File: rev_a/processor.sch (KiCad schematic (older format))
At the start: 1 part

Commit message: More work on processor schematic.
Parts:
- added C? (x2): C_VERT, symbol C_VERT
- added J?: TERMINATE_JUMPER, symbol TERMINATE_JUMPER
- added N?: BUS_MASTER_HEADER, symbol BUS_MASTER_HEADER
- added N?: FTDI_HEADER, symbol FTDI_HEADER
- added R? (x3): R_VERT, symbol R_VERT
- added R? (x3): R_HORIZ, symbol R_HORIZ
- added U?: MCP2562, symbol MCP2562
- added U? (x2): 74x06, symbol 74x06
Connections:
- net A1: now also U?.21 (PD7/OC2A)
- net D0: now also R?.2
- net D1: now also R?.2
- net D5: now also U?.18 (PD4/OC1B)
- net GND: now also U?.7 (GND), U?.7 (GND)
- net at U?.16 (PD2/RXD1/INT0): now also U?.1, U?.1 (TXD)
- net at U?.17 (PD3/TXD1/INT1): now also U?.4 (RXD)
- net at U?.9 (~RESET): now also C?.1, N?.6 (~RTS), R?.1, U?.2
- new net: N?.1 (LPWR1), N?.2 (LPWR2)
- new net: N?.10 (BPWR2), N?.9 (BPWR1)
- new net: N?.3 (LGND1), N?.4 (LGND2)
- new net: J?.1 (ON), N?.5 (CANH), U?.7 (CANH)
- new net: N?.6 (CANL), R?.2, U?.6 (CANL)
- new net: N?.7 (BGND1), N?.8 (BGND2)
- new net: R?.1, U?.2
- new net: C?.1, R?.1, R?.2, U?.1
- new net: N?.4 (TXD), R?.1
- new net: N?.5 (RXD), R?.1
- new net: J?.2 (COM), R?.1
- new net VCC: U?.14 (VCC), U?.14 (VCC)
- no-connect marks 0 -> 3

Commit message: Added some more symbols to library.
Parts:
- added H? (x4): 3MM_HOLE, symbol 3MM_HOLE
- added N? (x2): POWER_TERMINAL, symbol POWER_TERMINAL
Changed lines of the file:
@@
 NoConn ~ 1300 2900
 NoConn ~ 1300 5000
+$Comp
+L 3MM_HOLE H?
+U 1 1 53933893
+P 9800 4700
+F 0 "H?" H 9750 4850 50  0000 C CNN
+F 1 "3MM_HOLE" H 9800 4550 50  0000 C CNN
+F 2 "" H 9800 4700 60  0000 C CNN
+F 3 "" H 9800 4700 60  0000 C CNN
+	1    9800 4700
+	1    0    0    -1
+$EndComp
+$Comp
+L 3MM_HOLE H?
+U 1 1 539338AF
+P 9800 5100
+F 0 "H?" H 9750 5250 50  0000 C CNN
+F 1 "3MM_HOLE" H 9800 4950 50  0000 C CNN
+F 2 "" H 9800 5100 60  0000 C CNN
+F 3 "" H 9800 5100 60  0000 C CNN
+	1    9800 5100
+	1    0    0    -1
+$EndComp
+$Comp
+L 3MM_HOLE H?
+U 1 1 539338BA
+P 9800 5500
+F 0 "H?" H 9750 5650 50  0000 C CNN
+F 1 "3MM_HOLE" H 9800 5350 50  0000 C CNN
+F 2 "" H 9800 5500 60  0000 C CNN
+F 3 "" H 9800 5500 60  0000 C CNN
+	1    9800 5500
+	1    0    0    -1
+$EndComp
+$Comp
+L 3MM_HOLE H?
+U 1 1 539338C5
+P 9800 5900
+F 0 "H?" H 9750 6050 50  0000 C CNN
+F 1 "3MM_HOLE" H 9800 5750 50  0000 C CNN
+F 2 "" H 9800 5900 60  0000 C CNN
+F 3 "" H 9800 5900 60  0000 C CNN
+	1    9800 5900
+	1    0    0    -1
+$EndComp
+$Comp
+L POWER_TERMINAL N?
+U 1 1 539338DC
+P 9800 3750
+F 0 "N?" H 9750 3900 50  0000 C CNN
+F 1 "POWER_TERMINAL" H 9800 3600 50  0000 C CNN
+F 2 "" H 9800 3750 60  0000 C CNN
+F 3 "" H 9800 3750 60  0000 C CNN
+	1    9800 3750
+	1    0    0    -1
+$EndComp
+$Comp
+L POWER_TERMINAL N?
+U 1 1 539338EE
+P 9800 3350
+F 0 "N?" H 9750 3500 50  0000 C CNN
+F 1 "POWER_TERMINAL" H 9800 3200 50  0000 C CNN
+F 2 "" H 9800 3350 60  0000 C CNN
+F 3 "" H 9800 3350 60  0000 C CNN
+	1    9800 3350
+	1    0    0    -1
+$EndComp
 $EndSCHEMATC

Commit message: Making progress on processor sheet.
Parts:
- removed C?: C_VERT, symbol C_VERT
- removed N? (x2): POWER_TERMINAL, symbol POWER_TERMINAL
- added C? (x2): 18pF, symbol C_VERT
- added C?: .1uF, symbol C_HORIZ
- added C? (x3): .1uF, symbol C_VERT
- added D?: SCHOTTKY_DIODE_VERT, symbol SCHOTTKY_DIODE_VERT
- added R?: 1K, symbol R_VERT
- added SW?: 2_LEAD_PUSH_BUTTON, symbol 2_LEAD_PUSH_BUTTON
- added U? (x2): LM2940, symbol LM2940
- added X?: 16MHz, symbol CRYSTAL
- C?: value C_VERT -> .1uF
- R? (x2): value R_VERT -> 10K
- R?: value R_HORIZ -> 180
- R?: value R_VERT -> 120 1%
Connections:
- net labels added: +3.3V, +5V
- wire segments 129 -> 168
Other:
- moved on the sheet: C?, J?, N?, R?, U?, U?A

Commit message: Initial mounting hole layout is done.
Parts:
- removed N?: BUS_MASTER_HEADER, symbol BUS_MASTER_HEADER
- removed N?: FTDI_HEADER, symbol FTDI_HEADER
- removed U?: ATMEGA324_DIP40, symbol ATMEGA324_DIP40
- removed U?: MCP2562, symbol MCP2562
- removed U? (x2): LM2940, symbol LM2940
- added N8: BUS_SLAVE_HEADER, symbol BUS_SLAVE_HEADER
- added N9: FTDI_HEADER, symbol FTDI_HEADER
- added U1, U3: VOLTAGE_REGULATOR, symbol VOLTAGE_REGULATOR
- added U2: MCP2562, symbol MCP2562
- added U5: ATMEGA324_DIP40, symbol ATMEGA324_DIP40
- H6: renamed from H?; value 3MM_HOLE -> BASE_NE_3MM_HOLE
- H7: renamed from H?; value 3MM_HOLE -> BASE_NW_3MM_HOLE
- H8: renamed from H?; value 3MM_HOLE -> BASE_SE_3MM_HOLE
- H9: renamed from H?; value 3MM_HOLE -> BASE_SW_3MM_HOLE
- gave numbers to parts that had none: 19
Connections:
- net VCC is gone; now on net +5V: U4.14 (VCC), U4.14 (VCC)
- net +3.3V: now also U3.3 (VOUT)
- net +5V: now also U1.3 (VOUT), U2.3 (VDD), U2.5 (VIO), U3.1 (VIN), U5.10 (VCC), U5.30 (AVCC)
- net A0: now also U5.40 (PA0/ADC0)
- net A1: now also U5.39 (PA1/ADC1)
- net A2: now also U5.38 (PA2/ADC2)
- net A3: now also U5.37 (PA3/ADC3)
- net A4: now also U5.23 (PC1/SDA), U5.36 (PA4/ADC4)
- net A5: now also U5.22 (PC0/SCL), U5.35 (PA5/ADC5)
- net AREF: now also U5.32 (AREF)
- net D0: now also U5.14 (PD0/RXD0)
- net D1: now also U5.15 (PD1/TXD0)
- net D10: now also U5.5 (PB4/OC0B/SS)
- net D11: now also U5.6 (PB5/MOSI)
- net D12: now also U5.7 (PB6/MISO)
- net D13: now also U5.8 (PB7/SCK)
- net D2: now also U5.3 (PB2/INT2)
- net D3: now also U5.20 (PD6/OC2B)
- net D4: now also U5.1 (PB0/T0)
- net D5: now also U5.18 (PD4/OC1B), U5.2 (PB1/T1)
- net D6: now also U5.4 (PB3/OC0A)
- net D7: now also U5.34 (PA6/ADC6)
- net D8: now also U5.33 (PA7/ADC7)
- net D9: now also U5.19 (PD5/OC1A)
- net GND: now also N8.3 (LGND1), N8.4 (LGND2), N9.1 (GND), U1.2, U2.2 (VSS), U2.8 (STBY), U3.2, U5.11 (GND), U5.31 (GND)
- net MGND: now also N8.10 (BPWR2), N8.9 (BPWR1)
- net MPWR: now also N8.7 (BGND1), N8.8 (BGND2)
- net VIN: now also N8.1 (LPWR1), N8.2 (LPWR2), U1.1 (VIN)
- net ~RESET: now also U4.4, U5.9 (~RESET); no longer U4.2
- net at C2.1, X1.1: now also U5.12 (XTAL2)
- net at C4.1, X1.2: now also U5.13 (XTAL1)
- net at R3.2, U4.1: now also U2.1 (TXD), U5.16 (PD2/RXD1/INT0)
- net at R2.2: now also U2.4 (RXD), U5.17 (PD3/TXD1/INT1)
- net at J1.2 (COM): now also N8.5 (CANH), U2.7 (CANH)
- net at R1.2: now also N8.6 (CANL), U2.6 (CANL)
- net at C7.1, R5.2, R6.1: now also U4.3; no longer U4.1
- net at R3.1: now also N9.4 (TXD)
- net at R2.1: now also N9.5 (RXD)
- net at C6.1, R4.2: now also N9.6 (~RTS)
- no-connect marks 3 -> 10

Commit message: Worked on board.
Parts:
- R2, R3: value R_HORIZ -> 1K
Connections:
- net D0: now also R3.2
- net D1: now also R2.2
- net at U2.1 (TXD), U4.1, U5.16 (PD2/RXD1/INT0): no longer R3.2
- net at U2.4 (RXD), U5.17 (PD3/TXD1/INT1): no longer R2.2
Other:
- moved on the sheet: C1, C2, C3, C4, C5, N9, R2, R3, R4, U1, U3, X1

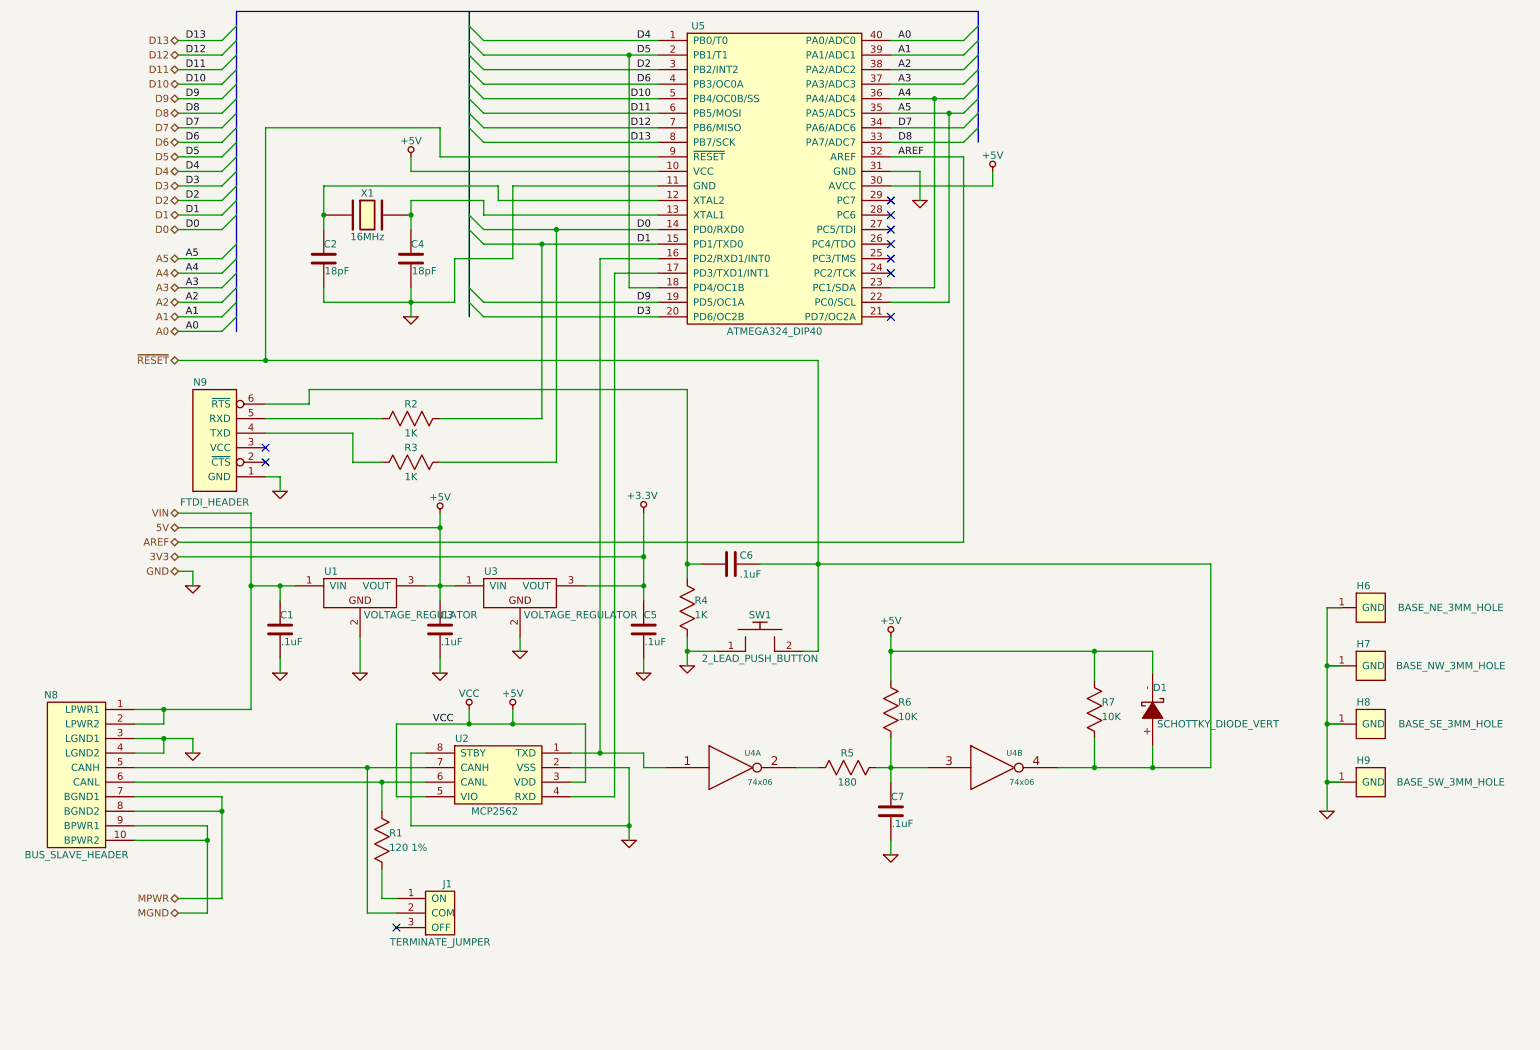
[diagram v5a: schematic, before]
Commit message: Busino passes DRC.
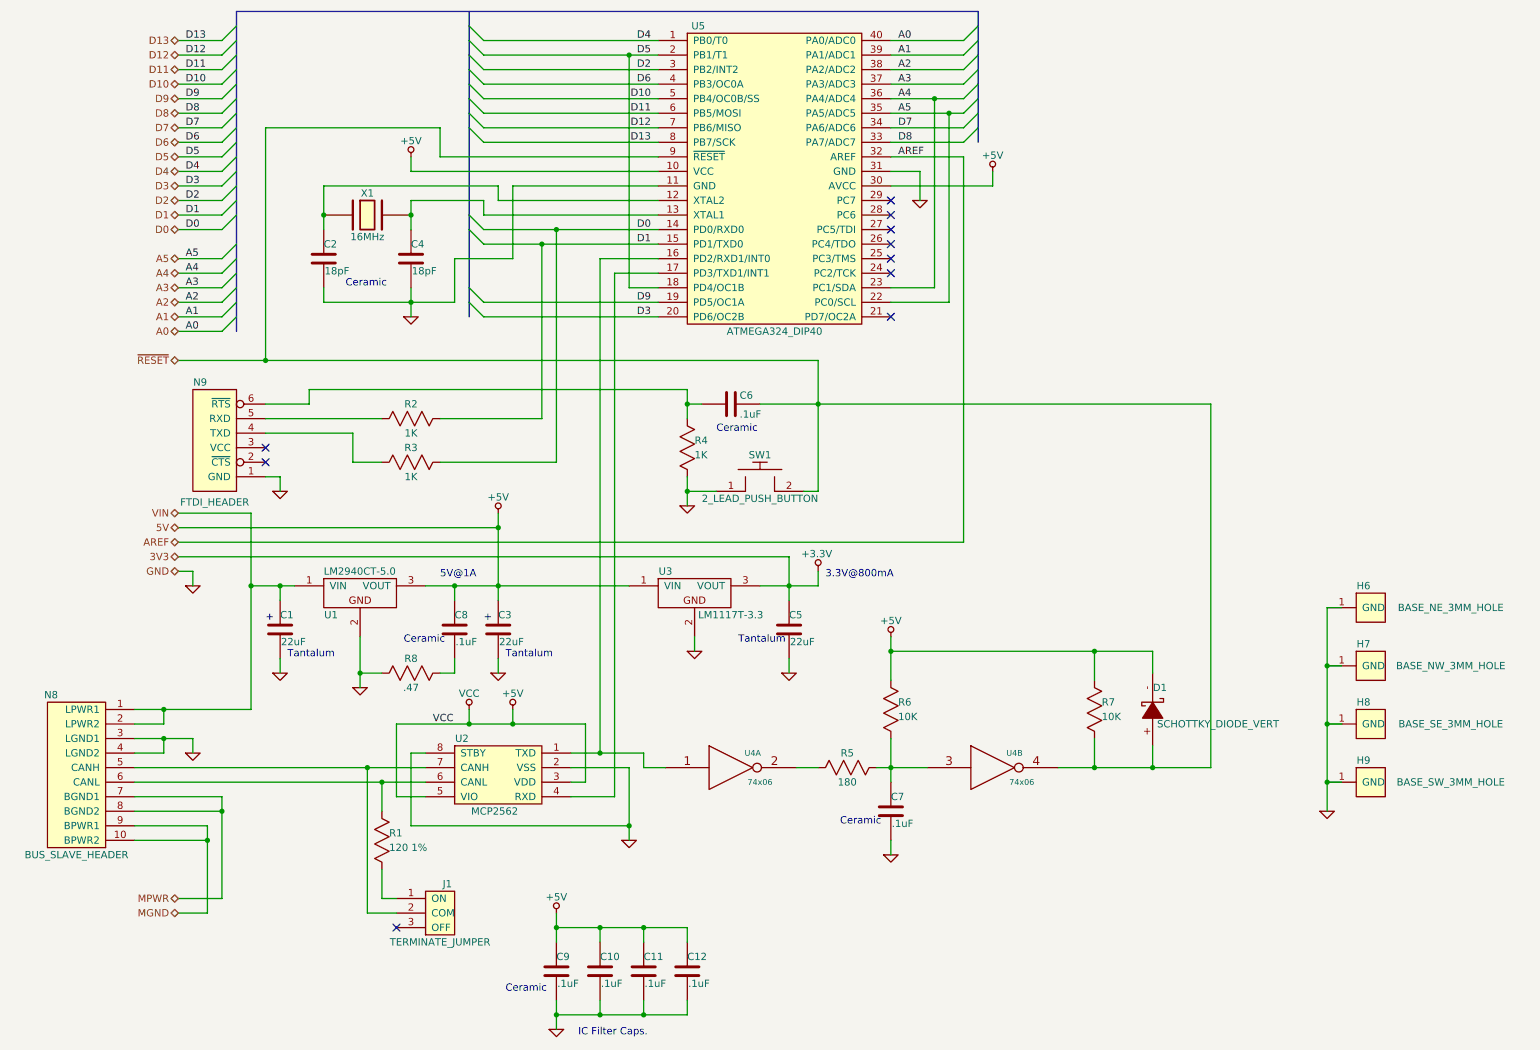
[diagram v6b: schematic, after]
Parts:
- added C10, C11, C12, C8, C9: .1uF, symbol C_VERT
- added R8: .47, symbol R_HORIZ
- C1, C3, C5: value .1uF -> 22uF
- U1: value VOLTAGE_REGULATOR -> LM2940CT-5.0
- U3: value VOLTAGE_REGULATOR -> LM1117T-3.3
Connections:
- net +5V: now also C10.1, C11.1, C12.1, C8.1, C9.1
- net GND: now also C10.2, C11.2, C12.2, C9.2, R8.1
- new net: C8.2, R8.2
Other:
- note added: "+"
- note added: "3.3V@800mA"
- note added: "5V@1A"
- note added: "Ceramic"
- note added: "IC Filter Caps."
- note added: "Tantalum"
- moved on the sheet: C3, C5, C6, R4, SW1, U3

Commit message: Rev. A of the Busino board layout is in pretty good shape.
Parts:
- added N16: AVR_JTAG_CONNECTOR, symbol AVR_JTAG_CONNECTOR
- added X2: OSHW_LOGO, symbol OSHW_LOGO
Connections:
- net +5V: now also N16.4 (VTREF)
- net GND: now also N16.10 (GND), N16.2 (GND)
- net ~RESET: now also N16.6 (~NRST)
- net at U5.24 (PC2/TCK): now also N16.1 (TCK)
- net at U5.25 (PC3/TMS): now also N16.5 (TMS)
- net at U5.26 (PC4/TDO): now also N16.3 (TDO)
- net at U5.27 (PC5/TDI): now also N16.9 (TDI)
- no-connect marks 10 -> 6
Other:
- moved on the sheet: H6, H7, H8, H9
